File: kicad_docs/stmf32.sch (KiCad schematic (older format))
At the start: 3 parts, among them U5 STM32F103RBTx

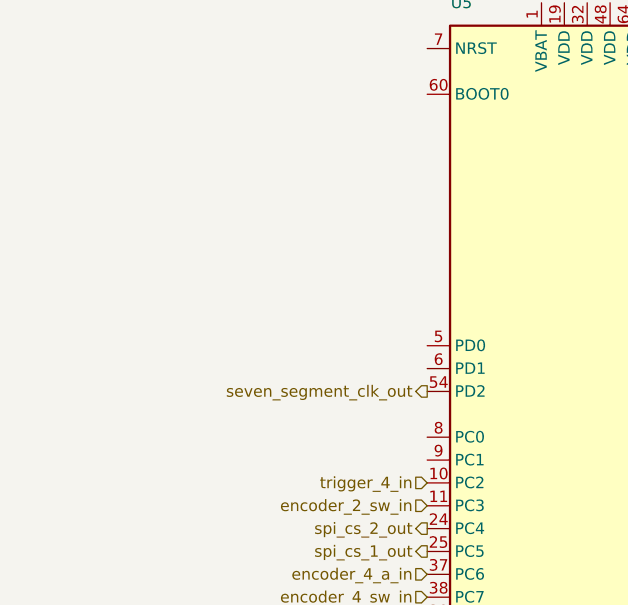
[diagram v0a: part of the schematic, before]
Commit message: change encoder push-button switch passives
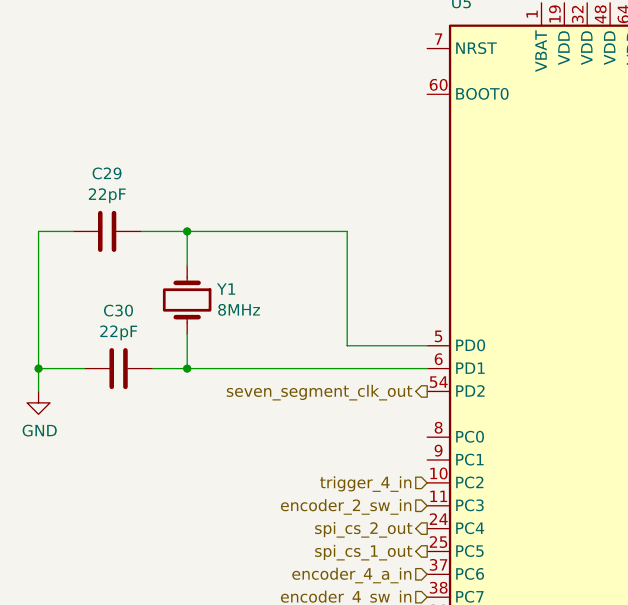
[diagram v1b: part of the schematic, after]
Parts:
- added C29, C30: 22pF, Capacitor_SMD:C_0805_2012Metric_Pad1.15x1.40mm_HandSolder, symbol Device:C
- added Y1: 8MHz, Crystal:Crystal_HC49-U_Vertical, symbol Device:Crystal
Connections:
- net GND: now also C29.2, C30.2
- net at U5.5 (PD0): now also C29.1, Y1.1
- net at U5.6 (PD1): now also C30.1, Y1.2
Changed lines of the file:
@@
 Text Label 7350 3400 0    50   ~ 0
 status_led
+$Comp
+L Device:Crystal Y1
+U 1 1 5E725775
+P 2850 2700
+F 0 "Y1" V 2804 2831 50  0000 L CNN
+F 1 "8MHz" V 2895 2831 50  0000 L CNN
+F 2 "Crystal:Crystal_HC49-U_Vertical" H 2850 2700 50  0001 C CNN
+F 3 "~" H 2850 2700 50  0001 C CNN
+	1    2850 2700
+	0    1    1    0
+$EndComp
+$Comp
+L Device:C C29
+U 1 1 5E725E75
+P 2500 2400
+F 0 "C29" V 2248 2400 50  0000 C CNN
+F 1 "22pF" V 2339 2400 50  0000 C CNN
+F 2 "Capacitor_SMD:C_0805_2012Metric_Pad1.15x1.40mm_HandSolder" H 2538 2250 50  0001 C CNN
+F 3 "~" H 2500 2400 50  0001 C CNN
+	1    2500 2400
+	0    1    1    0
+$EndComp
+$Comp
+L Device:C C30
+U 1 1 5E726505
+P 2550 3000
+F 0 "C30" V 2298 3000 50  0000 C CNN
+F 1 "22pF" V 2389 3000 50  0000 C CNN
+F 2 "Capacitor_SMD:C_0805_2012Metric_Pad1.15x1.40mm_HandSolder" H 2588 2850 50  0001 C CNN
+F 3 "~" H 2550 3000 50  0001 C CNN
+	1    2550 3000
+	0    1    1    0
+$EndComp
+Wire Wire Line
+	2850 2550 2850 2400
+Wire Wire Line
+	2850 2400 2650 2400
+Wire Wire Line
+	2850 2850 2850 3000
+Wire Wire Line
+	2850 3000 2700 3000
+Wire Wire Line
+	2400 3000 2200 3000
+Wire Wire Line
+	2200 3000 2200 2400
+Wire Wire Line
+	2200 2400 2350 2400
+Wire Wire Line
+	3900 3000 2850 3000
+Connection ~ 2850 3000
+Wire Wire Line
+	3900 2900 3550 2900
+Wire Wire Line
+	3550 2900 3550 2400
+Wire Wire Line
+	3550 2400 2850 2400
+Connection ~ 2850 2400
+$Comp
+L power:GND #PWR058
+U 1 1 5E72B044
+P 2200 3100
+F 0 "#PWR058" H 2200 2850 50  0001 C CNN
+F 1 "GND" H 2205 2927 50  0000 C CNN
+F 2 "" H 2200 3100 50  0001 C CNN
+F 3 "" H 2200 3100 50  0001 C CNN
+	1    2200 3100
+	1    0    0    -1
+$EndComp
+Wire Wire Line
+	2200 3100 2200 3000
+Connection ~ 2200 3000
 $EndSCHEMATC

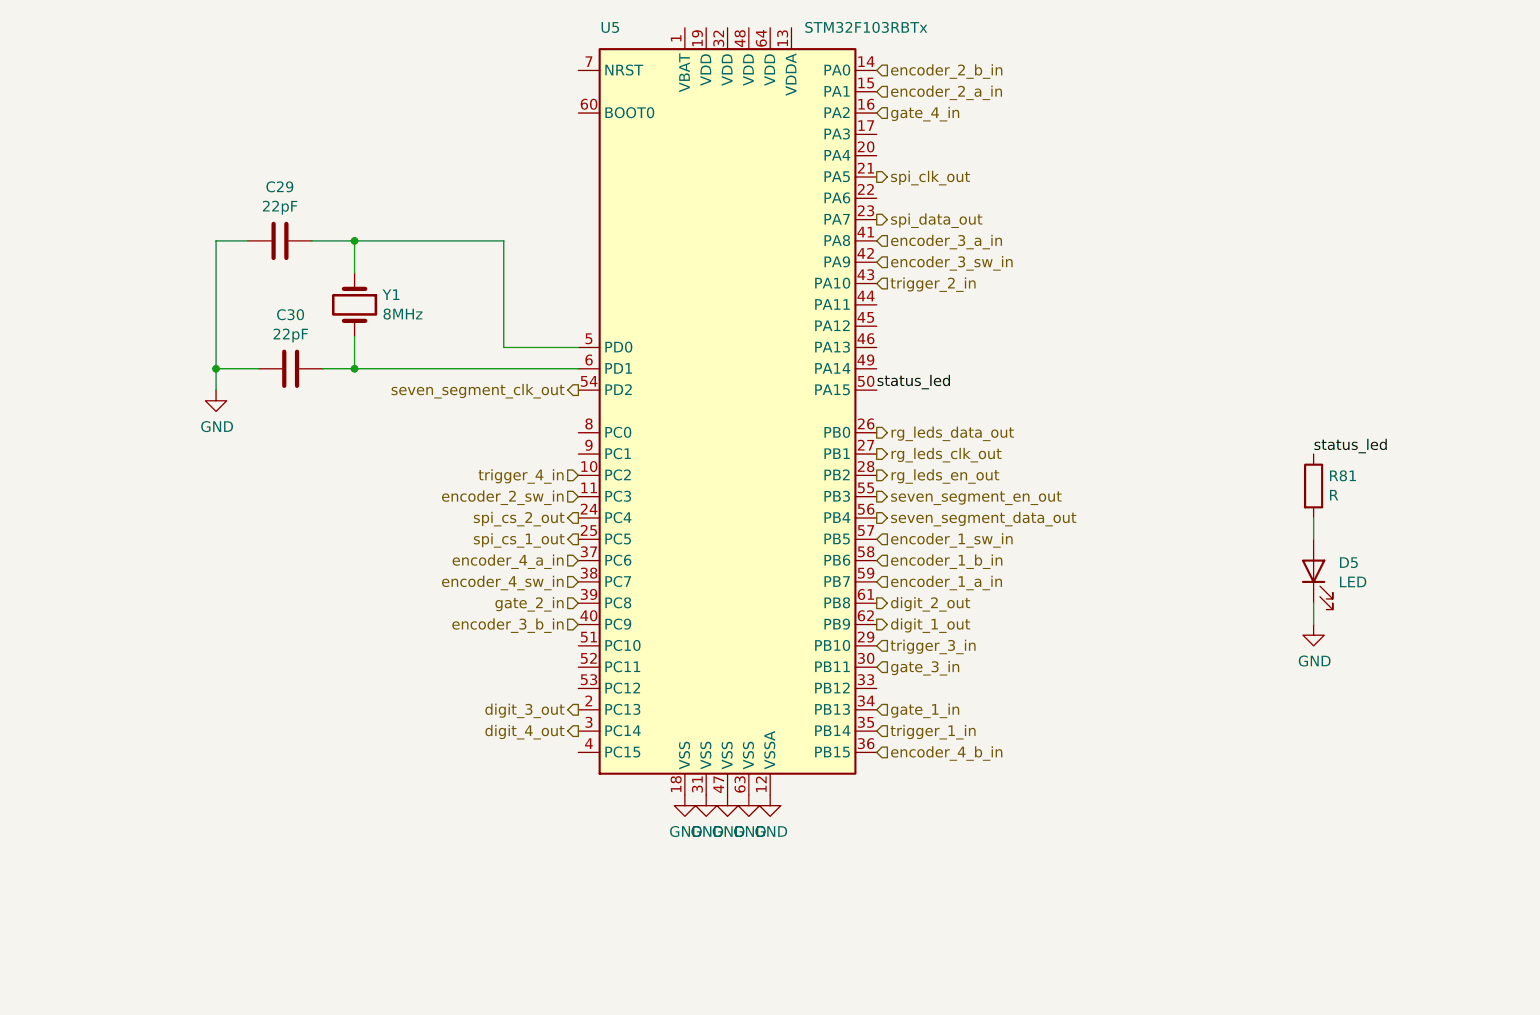
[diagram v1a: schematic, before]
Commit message: add EEPROM, big pcb re-design
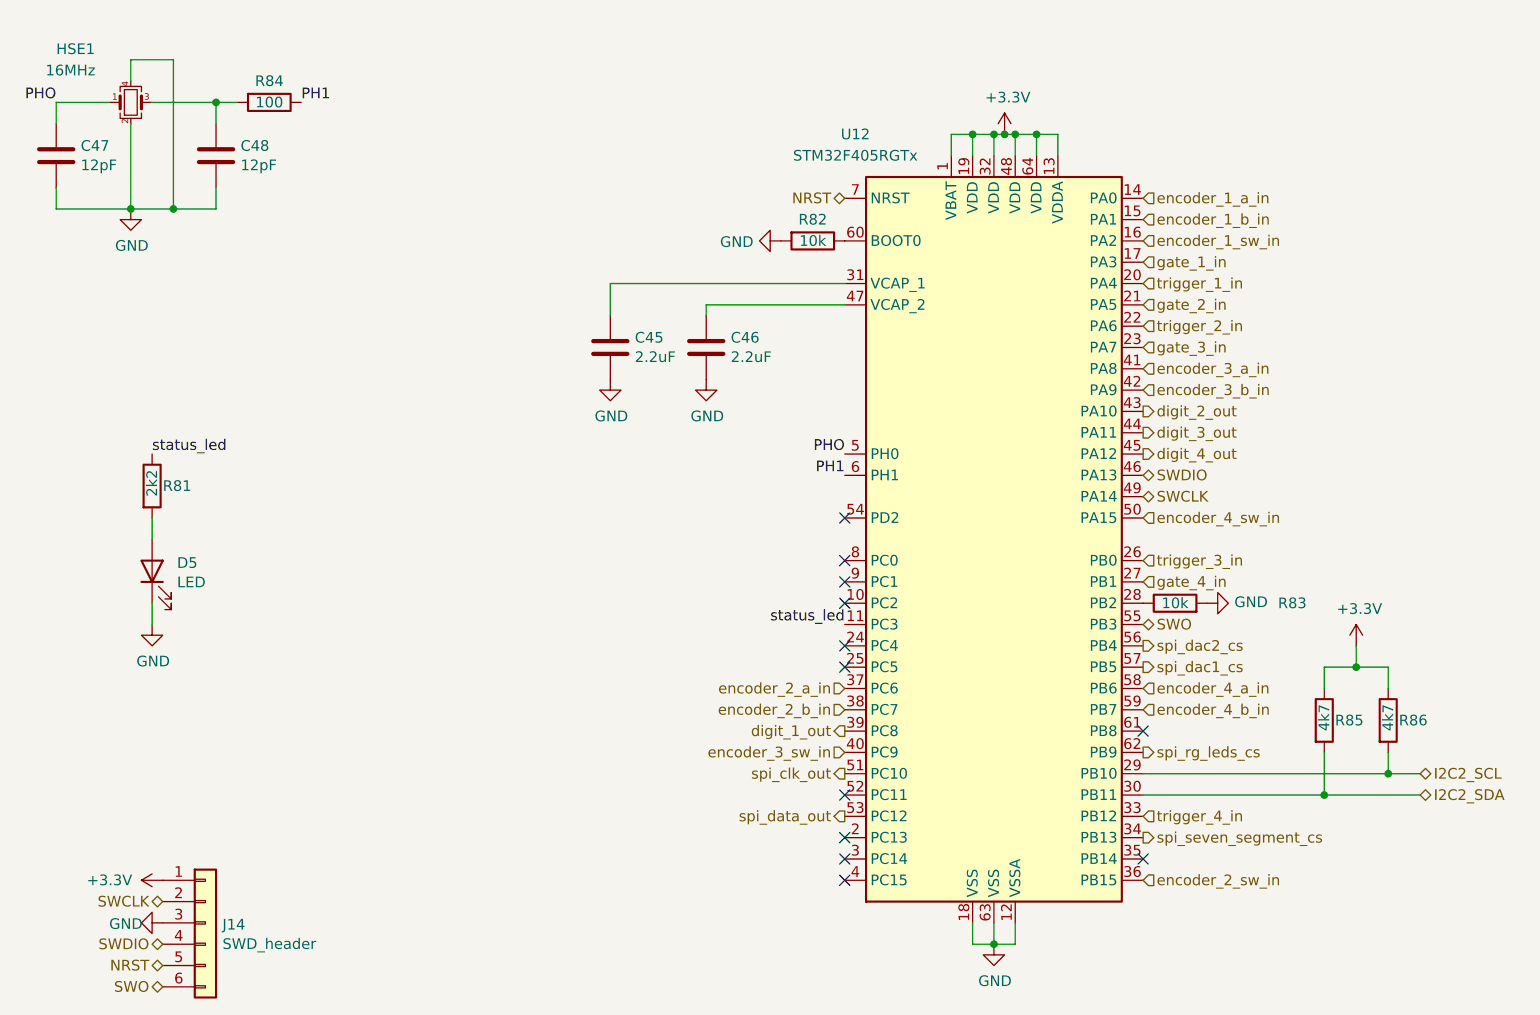
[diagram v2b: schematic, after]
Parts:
- removed C29, C30: 22pF, Capacitor_SMD:C_0805_2012Metric_Pad1.15x1.40mm_HandSolder, symbol Device:C
- removed U5: STM32F103RBTx, Package_QFP:LQFP-64_10x10mm_P0.5mm, symbol MCU_ST_STM32F1:STM32F103RBTx
- removed Y1: 8MHz, Crystal:Crystal_HC49-U_Vertical, symbol Device:Crystal
- added C45, C46: 2.2uF, Capacitor_SMD:C_0603_1608Metric, symbol Device:C
- added C47, C48: 12pF, Capacitor_SMD:C_0402_1005Metric, symbol Device:C
- added HSE1: 16MHz, Crystal:Crystal_SMD_3225-4Pin_3.2x2.5mm, symbol Device:Crystal_GND24_Small
- added J14: SWD_header, Connector_PinHeader_2.54mm:PinHeader_1x06_P2.54mm_Vertical, symbol Connector_Generic:Conn_01x06
- added R82, R83: 10k, Resistor_SMD:R_0402_1005Metric, symbol Device:R
- added R84: 100, Resistor_SMD:R_0402_1005Metric, symbol Device:R
- added R85, R86: 4k7, Resistor_SMD:R_0603_1608Metric, symbol Device:R
- added U12: STM32F405RGTx, Package_QFP:LQFP-64_10x10mm_P0.5mm, symbol MCU_ST_STM32F4:STM32F405RGTx
- D5: footprint LED_SMD:LED_0805_2012Metric_Pad1.15x1.40mm_HandSolder -> LED_SMD:LED_0603_1608Metric
- R81: value R -> 2k2; footprint Resistor_SMD:R_0805_2012Metric_Pad1.15x1.40mm_HandSolder -> Resistor_SMD:R_0603_1608Metric
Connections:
- net GND: now also C45.2, C46.2, C47.2, C48.2, HSE1.2, HSE1.4, J14.3 (Pin_3), R82.2, R83.2, U12.12 (VSSA), U12.18 (VSS), U12.63 (VSS)
- net digit_1_out: now also U12.39 (PC8)
- net digit_2_out: now also U12.43 (PA10)
- net digit_3_out: now also U12.44 (PA11)
- net digit_4_out: now also U12.45 (PA12)
- net encoder_1_a_in: now also U12.14 (PA0)
- net encoder_1_b_in: now also U12.15 (PA1)
- net encoder_1_sw_in: now also U12.16 (PA2)
- net encoder_2_a_in: now also U12.37 (PC6)
- net encoder_2_b_in: now also U12.38 (PC7)
- net encoder_2_sw_in: now also U12.36 (PB15)
- net encoder_3_a_in: now also U12.41 (PA8)
- net encoder_3_b_in: now also U12.42 (PA9)
- net encoder_3_sw_in: now also U12.40 (PC9)
- net encoder_4_a_in: now also U12.58 (PB6)
- net encoder_4_b_in: now also U12.59 (PB7)
- net encoder_4_sw_in: now also U12.50 (PA15)
- net gate_1_in: now also U12.17 (PA3)
- net gate_2_in: now also U12.21 (PA5)
- net gate_3_in: now also U12.23 (PA7)
- net gate_4_in: now also U12.27 (PB1)
- net spi_clk_out: now also U12.51 (PC10)
- net spi_data_out: now also U12.53 (PC12)
- net status_led: now also U12.11 (PC3)
- net trigger_1_in: now also U12.20 (PA4)
- net trigger_2_in: now also U12.22 (PA6)
- net trigger_3_in: now also U12.26 (PB0)
- net trigger_4_in: now also U12.33 (PB12)
- new net: R83.1, U12.28 (PB2)
- new net: C45.1, U12.31 (VCAP_1)
- new net: C46.1, U12.47 (VCAP_2)
- new net: R82.1, U12.60 (BOOT0)
- new net: C48.1, HSE1.3, R84.2
- new net +3V3: J14.1 (Pin_1), R85.1, R86.1, U12.1 (VBAT), U12.13 (VDDA), U12.19 (VDD), U12.32 (VDD), U12.48 (VDD), U12.64 (VDD)
- new net I2C2_SCL: R86.2, U12.29 (PB10)
- new net I2C2_SDA: R85.2, U12.30 (PB11)
- new net NRST: J14.5 (Pin_5), U12.7 (NRST)
- new net PH1: R84.1, U12.6 (PH1)
- new net PHO: C47.1, HSE1.1, U12.5 (PH0)
- new net SWCLK: J14.2 (Pin_2), U12.49 (PA14)
- new net SWDIO: J14.4 (Pin_4), U12.46 (PA13)
- new net SWO: J14.6 (Pin_6), U12.55 (PB3)
- new net spi_dac1_cs: U12.57 (PB5)
- new net spi_dac2_cs: U12.56 (PB4)
- new net spi_rg_leds_cs: U12.62 (PB9)
- new net spi_seven_segment_cs: U12.34 (PB13)
- no-connect marks 0 -> 12
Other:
- moved on the sheet: D5, R81
